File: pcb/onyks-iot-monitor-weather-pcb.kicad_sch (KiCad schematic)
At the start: 32 parts, among them J1 53398-0371, J10 Conn_01x02_Pin, J11 Conn_01x06_Pin, J12 Conn_02x05_Odd_Even, J13 Conn_01x02_Pin, J2 53398-0371, J3 53048-0810, J4 53398-0371, J5 53398-0371, J6 53398-0371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

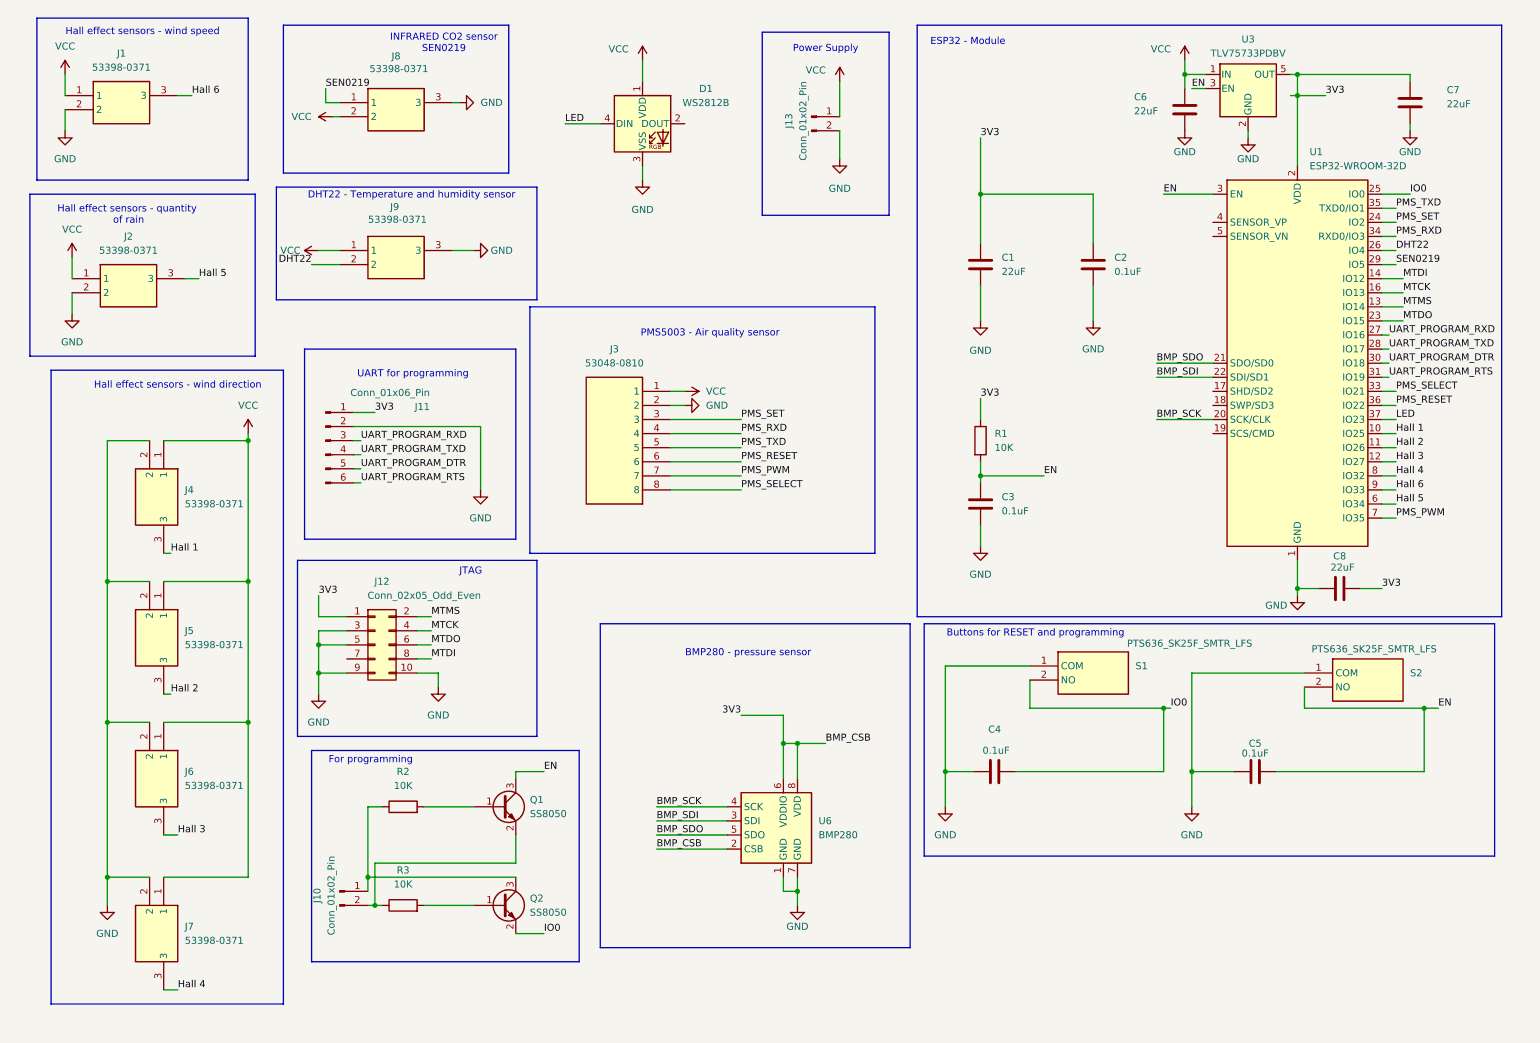
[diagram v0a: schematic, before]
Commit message: Aded Readme, change schematic layout, added block diagrams
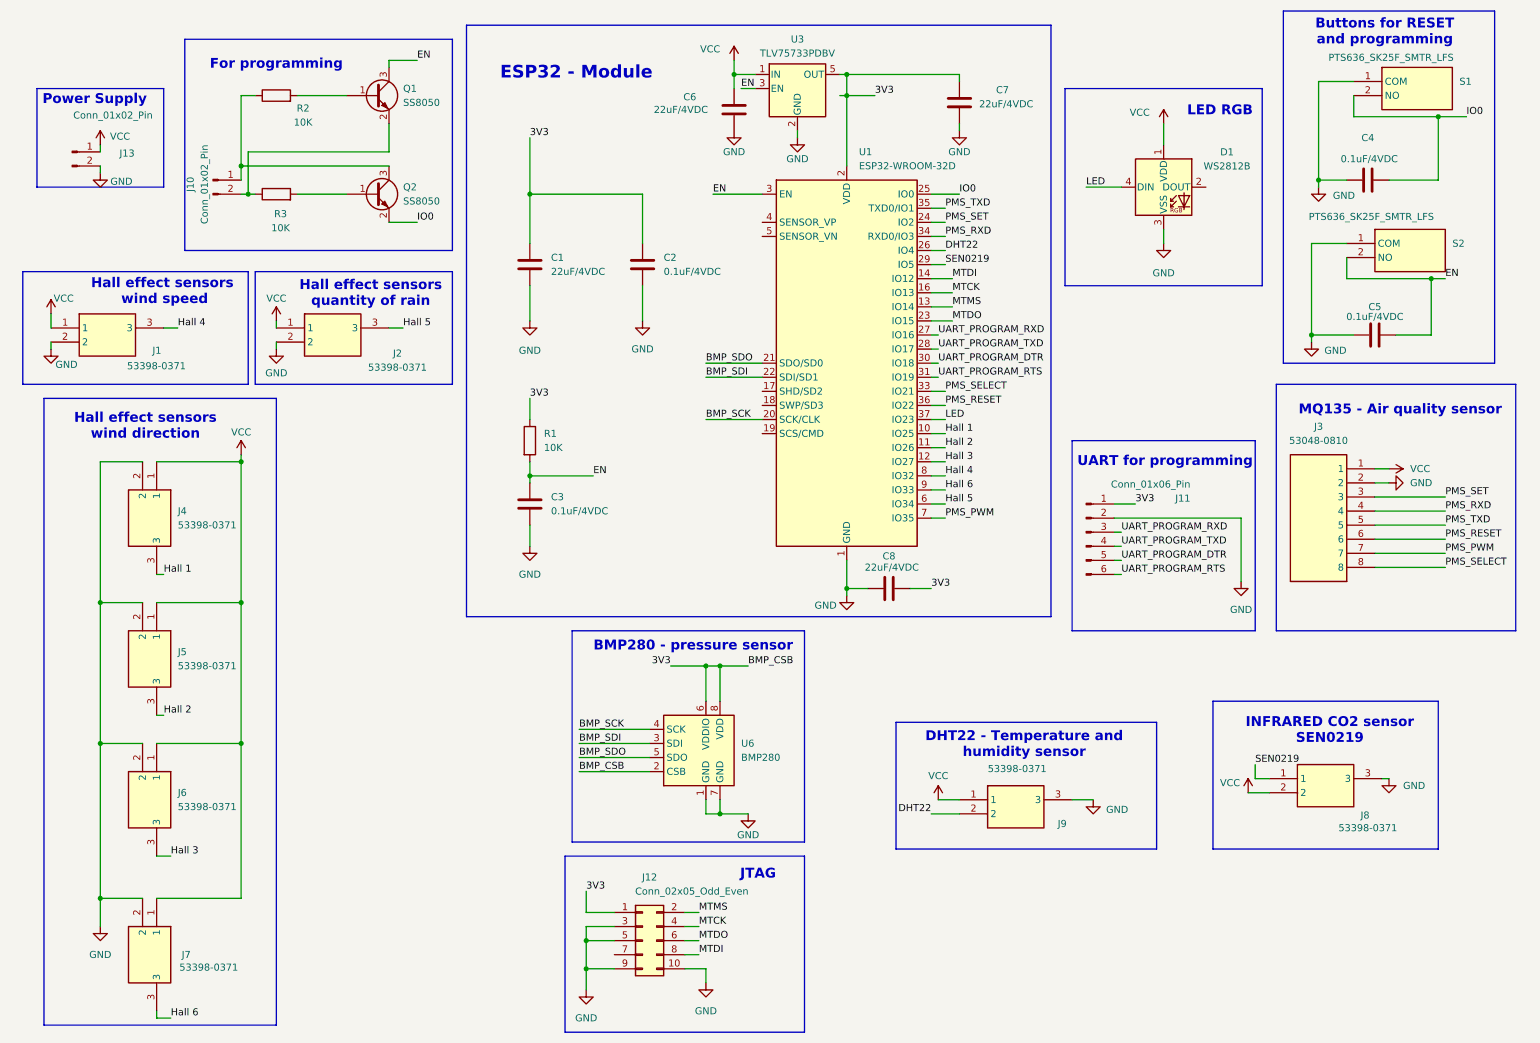
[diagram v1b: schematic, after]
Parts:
- C1, C6, C7, C8: value 22uF -> 22uF/4VDC
- C2, C3, C4, C5: value 0.1uF -> 0.1uF/4VDC
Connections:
- net Hall 4: now also J1.3; no longer J7.3
- net Hall 6: now also J7.3; no longer J1.3
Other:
- note added: "Hall effect sensors quantity of rain"
- note added: "Hall effect sensors wind direction"
- note added: "Hall effect sensors wind speed"
- note added: "LED RGB"
- note added: "MQ135 - Air quality sensor"
- note removed: "Hall effect sensors - quantity of rain"
- note removed: "Hall effect sensors - wind direction"
- note removed: "Hall effect sensors - wind speed"
- note removed: "PMS5003 - Air quality sensor"
- moved on the sheet: C1, C2, C3, C4, C5, C6, C7, C8, D1, J10, J11, J12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

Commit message: Poprawki w schemacie elektrycznym
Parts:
- removed C8: 22uF/4VDC, Capacitor_SMD:C_0603_1608Metric, symbol Device:C
- J1: footprint 1bmoje:53398-0371 -> 53398-0371; symbol 1BMoje:53398-0371 -> Connector:Conn_01x03_Pin
- J2, J4, J5, J6, J7, J8, J9: symbol 1BMoje:53398-0371 -> Connector:Conn_01x03_Pin
- S1, S2: symbol 1BMoje:PTS636_SK25F_SMTR_LFS -> Switch:SW_Push
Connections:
- net EN: no longer U3.3 (EN)
- net VCC: now also U3.3 (EN)
- net 3V3 renamed +3.3V
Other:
- note added: "Hall effect sensor quantity of rain"
- note added: "Hall effect sensor wind speed"
- note added: "Power Supply - Vcc : 5 V"
- note removed: "Hall effect sensors quantity of rain"
- note removed: "Hall effect sensors wind speed"
- note removed: "Power Supply"
- moved on the sheet: C4, C5, C6, C7, J10, J11, J13, J3, Q1, Q2, R2, R3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

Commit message: Poprawki w schemacie elektrycznym
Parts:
- added R10, R12, R14, R4, R6, R8: 470, Resistor_SMD:R_0603_1608Metric, symbol Device:R
- added R11, R13, R15, R5, R7, R9: 910, Resistor_SMD:R_0603_1608Metric, symbol Device:R
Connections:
- net GND: now also R11.2, R13.2, R15.2, R5.2, R7.2, R9.2
- net Hall 1: now also R8.2, R9.1; no longer J4.3 (Pin_3)
- net Hall 2: now also R10.2, R11.1; no longer J5.3 (Pin_3)
- net Hall 3: now also R12.2, R13.1; no longer J6.3 (Pin_3)
- net Hall 4: now also R4.2, R5.1; no longer J1.3 (Pin_3)
- net Hall 5: now also R6.2, R7.1; no longer J2.3 (Pin_3)
- net Hall 6: now also R14.2, R15.1; no longer J7.3 (Pin_3)
- new net: J1.3 (Pin_3), R4.1
- new net: J7.3 (Pin_3), R14.1
- new net: J2.3 (Pin_3), R6.1
- new net: J6.3 (Pin_3), R12.1
- new net: J5.3 (Pin_3), R10.1
- new net: J4.3 (Pin_3), R8.1
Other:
- moved on the sheet: J2, J4, J5, J6, J7

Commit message: Dalsze zmiany w schemacie elektrycznym - przewidywane duże zmiany w PCB
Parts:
- removed J10: Conn_01x02_Pin, Connector_PinHeader_2.54mm:PinHeader_1x02_P2.54mm_Vertical, symbol Connector:Conn_01x02_Pin
- removed J3: 53048-0810, 530480810, symbol 1BMoje:53048-0810
- added J3: Conn_01x04_Pin, 1bmoje:533980471- MOLEXx4, symbol Connector:Conn_01x04_Pin
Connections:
- net +3.3V: now also J3.4 (Pin_4)
- net GND: now also J3.3 (Pin_3)
- net IO0: now also Q2.3 (C); no longer Q2.2 (E)
- net UART_PROGRAM_DTR: now also Q2.2 (E), R2.1; no longer U1.30 (IO18)
- net UART_PROGRAM_RTS: now also Q1.2 (E), R3.1; no longer U1.31 (IO19)
- net PMS_PWM renamed MQ135_AOUT
- net MQ135_AOUT: now also J3.2 (Pin_2)
- net PMS_RESET renamed MQ135_DOUT
- net MQ135_DOUT: now also J3.1 (Pin_1)
- net PMS_RXD: no longer names the net of U1.34 (RXD0/IO3)
- net PMS_SELECT: no longer names the net of U1.33 (IO21)
- net PMS_SET: no longer names the net of U1.24 (IO2)
- net PMS_TXD: no longer names the net of U1.35 (TXD0/IO1)
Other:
- note added: "DHT22 - Temperature and humidity sensor: 3V3 signal logic"
- note added: "INFRARED CO2 sensor SEN0219 Output: 0.4 - 2 V"
- note added: "MQ135(Waveshare module) Air quality sensor"
- note removed: "DHT22 - Temperature and humidity sensor"
- note removed: "INFRARED CO2 sensor SEN0219"
- note removed: "MQ135 - Air quality sensor"
- moved on the sheet: J11, Q1, Q2, R2, R3

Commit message: Struktura hierarchiczna
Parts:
- removed C1, C6, C7: 22uF/4VDC, Capacitor_SMD:C_0603_1608Metric, symbol Device:C
- removed C2, C3: 0.1uF/4VDC, Capacitor_SMD:C_0603_1608Metric, symbol Device:C
- removed J1: 53398-0371, 53398-0371, symbol Connector:Conn_01x03_Pin
- removed J11: Conn_01x06_Pin, Connector_PinHeader_2.54mm:PinHeader_1x06_P2.54mm_Vertical, symbol Connector:Conn_01x06_Pin
- removed J12: Conn_02x05_Odd_Even, Connector_PinHeader_2.54mm:PinHeader_2x05_P2.54mm_Vertical, symbol Connector_Generic:Conn_02x05_Odd_Even
- removed J13: Conn_01x02_Pin, Connector_PinHeader_2.54mm:PinHeader_1x02_P2.54mm_Vertical, symbol Connector:Conn_01x02_Pin
- removed J2, J4, J5, J6, J7, J8, J9: 53398-0371, 1bmoje:53398-0371, symbol Connector:Conn_01x03_Pin
- removed J3: Conn_01x04_Pin, 1bmoje:533980471- MOLEXx4, symbol Connector:Conn_01x04_Pin
- removed Q1, Q2: SS8050, Package_TO_SOT_SMD:SOT-23, symbol Transistor_BJT:SS8050
- removed R1, R2, R3: 10K, Resistor_SMD:R_0603_1608Metric, symbol Device:R
- removed R10, R12, R14, R4, R6, R8: 470, Resistor_SMD:R_0603_1608Metric, symbol Device:R
- removed R11, R13, R15, R5, R7, R9: 910, Resistor_SMD:R_0603_1608Metric, symbol Device:R
- removed U1: ESP32-WROOM-32D, RF_Module:ESP32-WROOM-32D, symbol RF_Module:ESP32-WROOM-32D
- removed U3: TLV75733PDBV, Package_TO_SOT_SMD:SOT-23-5, symbol Regulator_Linear:TLV75733PDBV
- removed U6: BMP280, Package_LGA:Bosch_LGA-8_2x2.5mm_P0.65mm_ClockwisePinNumbering, symbol Sensor_Pressure:BMP280
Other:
- added sheet Power Supply and ESP32 (PowerSupplyESP.kicad_sch)
- added sheet Programming and Debuging (Programming.kicad_sch)
- added sheet Sensors (Sensors.sch.kicad_sch)
- note removed: "BMP280 - pressure sensor"
- note removed: "DHT22 - Temperature and humidity sensor: 3V3 signal logic"
- note removed: "ESP32 - Module"
- note removed: "For programming"
- note removed: "Hall effect sensor quantity of rain"
- note removed: "Hall effect sensor wind speed"
- note removed: "Hall effect sensors wind direction"
- note removed: "INFRARED CO2 sensor SEN0219 Output: 0.4 - 2 V"
- note removed: "JTAG"
- note removed: "MQ135(Waveshare module) Air quality sensor"
- note removed: "Power Supply - Vcc : 5 V"
- note removed: "UART for programming"
- moved on the sheet: C4, C5, D1, S1, S2

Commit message: Drobne poprawki w schemacie elektrycznym
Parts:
- removed C4, C5: 0.1uF/4VDC, Capacitor_SMD:C_0603_1608Metric, symbol Device:C
- removed D1: WS2812B, LED_SMD:LED_WS2812B_PLCC4_5.0x5.0mm_P3.2mm, symbol LED:WS2812B
- removed S1, S2: PTS636_SK25F_SMTR_LFS, 1bmoje:PTS636SK25FSMTRLFS, symbol Switch:SW_Push
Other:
- sheet Power Supply and ESP32 renamed ESP32
- added sheet PowerSupply (PowerSupply.kicad_sch)
- sheet ESP32: file PowerSupplyESP.kicad_sch -> ESP.kicad_sch
- sheet ESP32 ports: added none; removed IO23
- note removed: "Buttons for RESET and programming"
- note removed: "LED RGB"

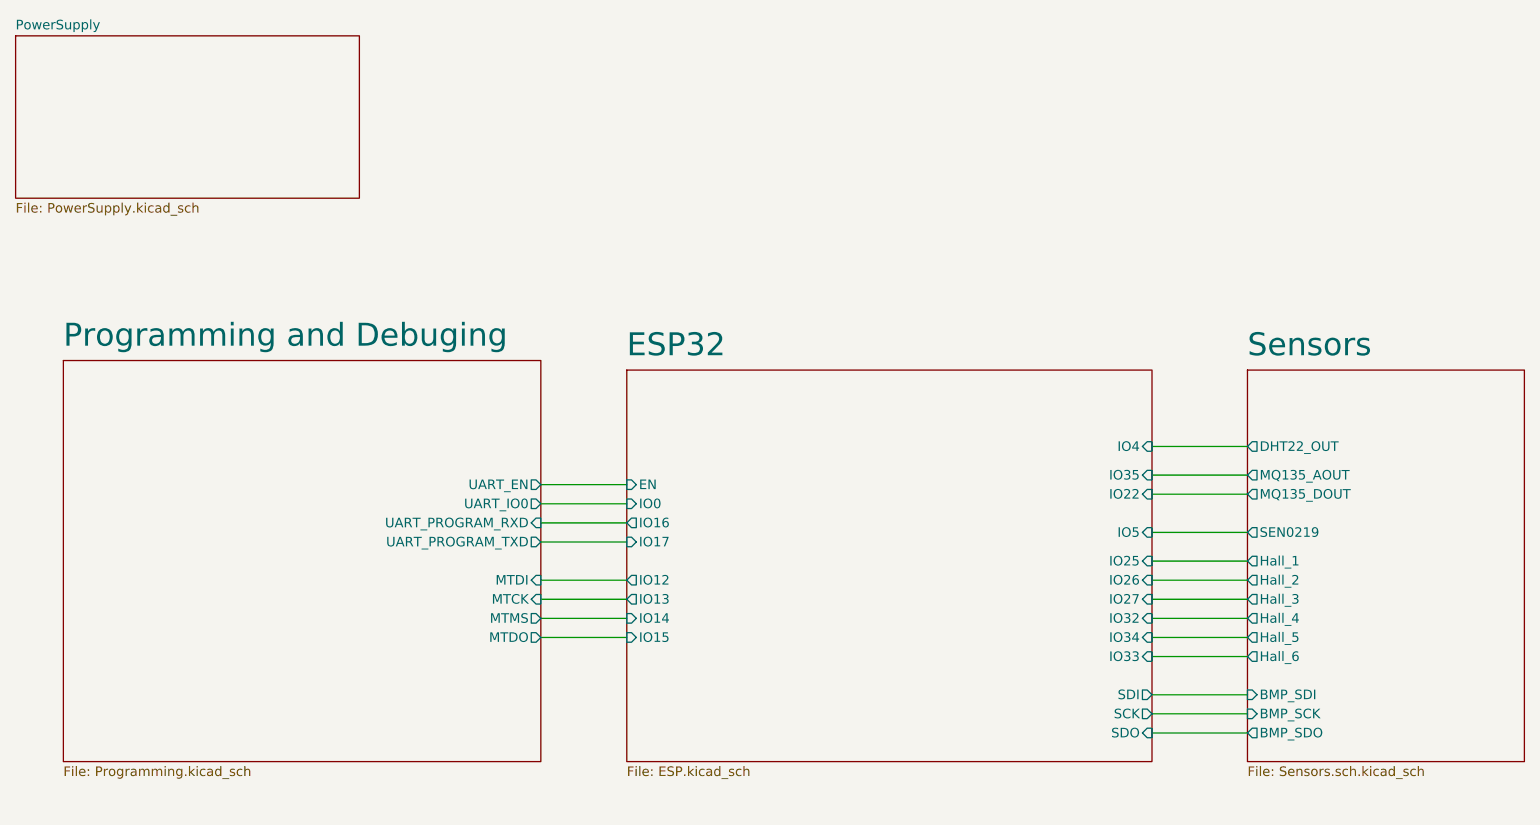
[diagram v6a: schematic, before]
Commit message: poprawiony schemat w pdf
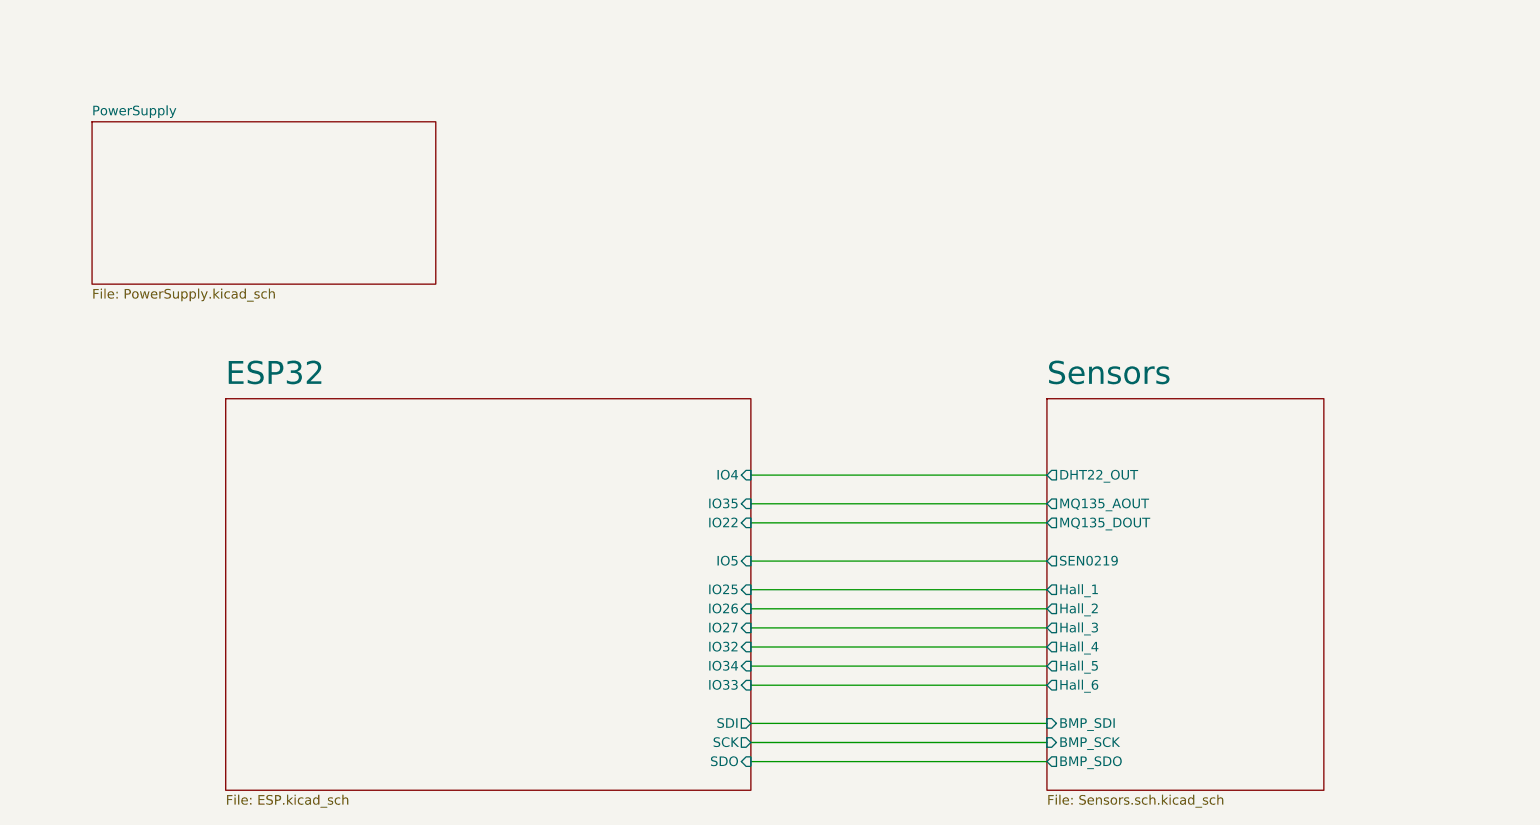
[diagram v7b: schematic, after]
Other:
- removed sheet Programming and Debuging
- sheet ESP32 ports: added none; removed EN, IO0, IO12, IO13, IO14, IO15, IO16, IO17
